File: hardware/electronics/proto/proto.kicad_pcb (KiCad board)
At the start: 2 copper layers, 47.9 x 53.5 mm, 49 parts, among them J1 Conn_01x08_Female, U1 ADS131M06IRSNT, U2 AP131-30

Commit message: Switch strain gauge footprints
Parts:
- R1, R10, R11, R12, R2, R3, R4, R5, R6, R7, R8, R9: value 1k -> 350; footprint Resistor_SMD:R_2512_6332Metric_Pad1.40x3.35mm_HandSolder -> proto:StrainGauge_BF350-3AA
- U1: value ADS131M06IRSNT -> ADS131M06

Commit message: Update layout and route
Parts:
- added R25: 3.9k, Resistor_SMD:R_0603_1608Metric_Pad0.98x0.95mm_HandSolder, F.Cu at (9.25, 4.95)
- added R26: 3.9k, Resistor_SMD:R_0603_1608Metric_Pad0.98x0.95mm_HandSolder, F.Cu at (9.25, -4.95)
- added R27: 3.9k, Resistor_SMD:R_0603_1608Metric_Pad0.98x0.95mm_HandSolder, F.Cu at (-0.34, -10.5)
- added R28: 3.9k, Resistor_SMD:R_0603_1608Metric_Pad0.98x0.95mm_HandSolder, F.Cu at (-8.91, -5.54)
- added R29: 3.9k, Resistor_SMD:R_0603_1608Metric_Pad0.98x0.95mm_HandSolder, F.Cu at (-8.91, 5.54)
- added R30: 3.9k, Resistor_SMD:R_0603_1608Metric_Pad0.98x0.95mm_HandSolder, F.Cu at (-0.34, 10.5)
- R13, R14, R15, R16, R17, R18, R19, R20, R21, R22, R23, R24: value 1k -> 8.2k
- moved R5 1.40 mm to (-6.07, -19.3), turned to 17.5 degrees
- moved R6 1.40 mm to (-6.07, -19.3), turned to -162.5 degrees
- moved R1 1.40 mm to (19.7, 4.37), turned to -102.5 degrees
- moved R2 1.40 mm to (19.7, 4.37), turned to 77.5 degrees
- moved R10 1.40 mm to (-13.6, 14.9), turned to -42.5 degrees
- moved R9 1.40 mm to (-13.6, 14.9), turned to 137.5 degrees
- moved R7 1.40 mm to (-13.6, -14.9), turned to 42.5 degrees
- moved R8 1.40 mm to (-13.6, -14.9), turned to -137.5 degrees
- moved R3 1.40 mm to (19.7, -4.37), turned to -77.5 degrees
- moved R4 1.40 mm to (19.7, -4.37), turned to 102.5 degrees
- moved R11 1.40 mm to (-6.07, 19.3), turned to 162.5 degrees
- moved R12 1.40 mm to (-6.07, 19.3), turned to -17.5 degrees
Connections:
- C1 pad 2: /BRa -> Net-(C1-Pad2)
- C2 pad 2: /BRb -> Net-(C2-Pad2)
- C3 pad 2: /BRc -> Net-(C3-Pad2)
- C4 pad 2: /BRd -> Net-(C4-Pad2)
- C5 pad 2: /BRe -> Net-(C5-Pad2)
- C6 pad 2: /BRf -> Net-(C6-Pad2)
- R11 pad 1: VDDA -> /BRf
- R11 pad 2: /BRf -> VDDA
- R12 pad 1: /BRf -> GNDA
- R12 pad 2: GNDA -> /BRf
- R3 pad 1: VDDA -> /BRb
- R3 pad 2: /BRb -> VDDA
- R4 pad 1: /BRb -> GNDA
- R4 pad 2: GNDA -> /BRb
- R7 pad 1: VDDA -> /BRd
- R7 pad 2: /BRd -> VDDA
- R8 pad 1: /BRd -> GNDA
- R8 pad 2: GNDA -> /BRd
- U1 pad 1: /BRc -> Net-(C3-Pad2)
- U1 pad 29: /BRa -> Net-(C1-Pad2)
- U1 pad 32: /BRb -> Net-(C2-Pad2)
- U1 pad 4: /BRd -> Net-(C4-Pad2)
- U1 pad 5: /BRe -> Net-(C5-Pad2)
- U1 pad 8: /BRf -> Net-(C6-Pad2)
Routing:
- net /BRa: track 34.6 -> 9.19 mm
- net Net-(C1-Pad2): track 0.00 -> 20.6 mm
- net /BRb: track 27.2 -> 9.19 mm
- net /BRc: track 24.8 -> 9.19 mm
- net /BRf: track 24.8 -> 9.19 mm
- net /BRe: track 23.5 -> 9.19 mm
- net /BRd: track 23.5 -> 9.19 mm
- net Net-(C2-Pad2): track 0.00 -> 13.2 mm
- net Net-(C6-Pad2): track 0.00 -> 10.8 mm
- net Net-(C3-Pad2): track 0.00 -> 10.8 mm
- net Net-(C4-Pad2): track 0.00 -> 9.55 mm
- net Net-(C5-Pad2): track 0.00 -> 9.55 mm
- net GNDA: track 67.6 -> 74.2 mm
- net VDDA: track 95.6 -> 102.0 mm

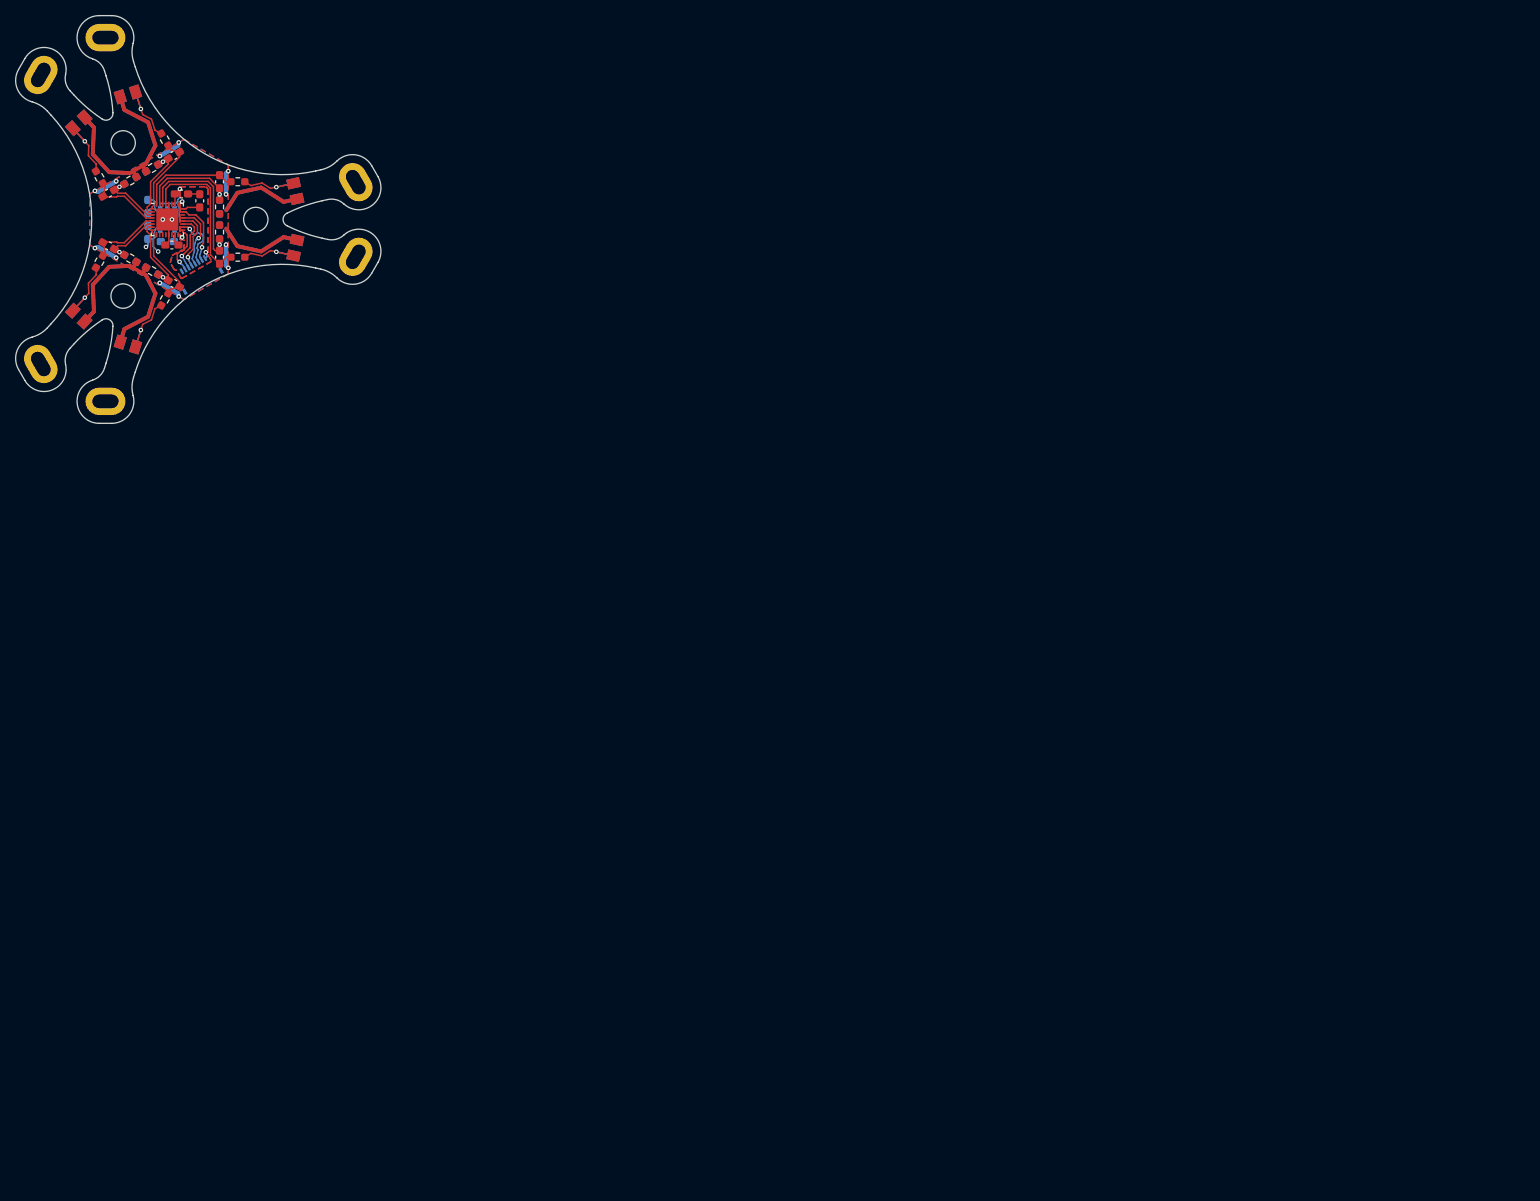
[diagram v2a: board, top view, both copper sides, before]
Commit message: Move prototype base PCB into center of sheet
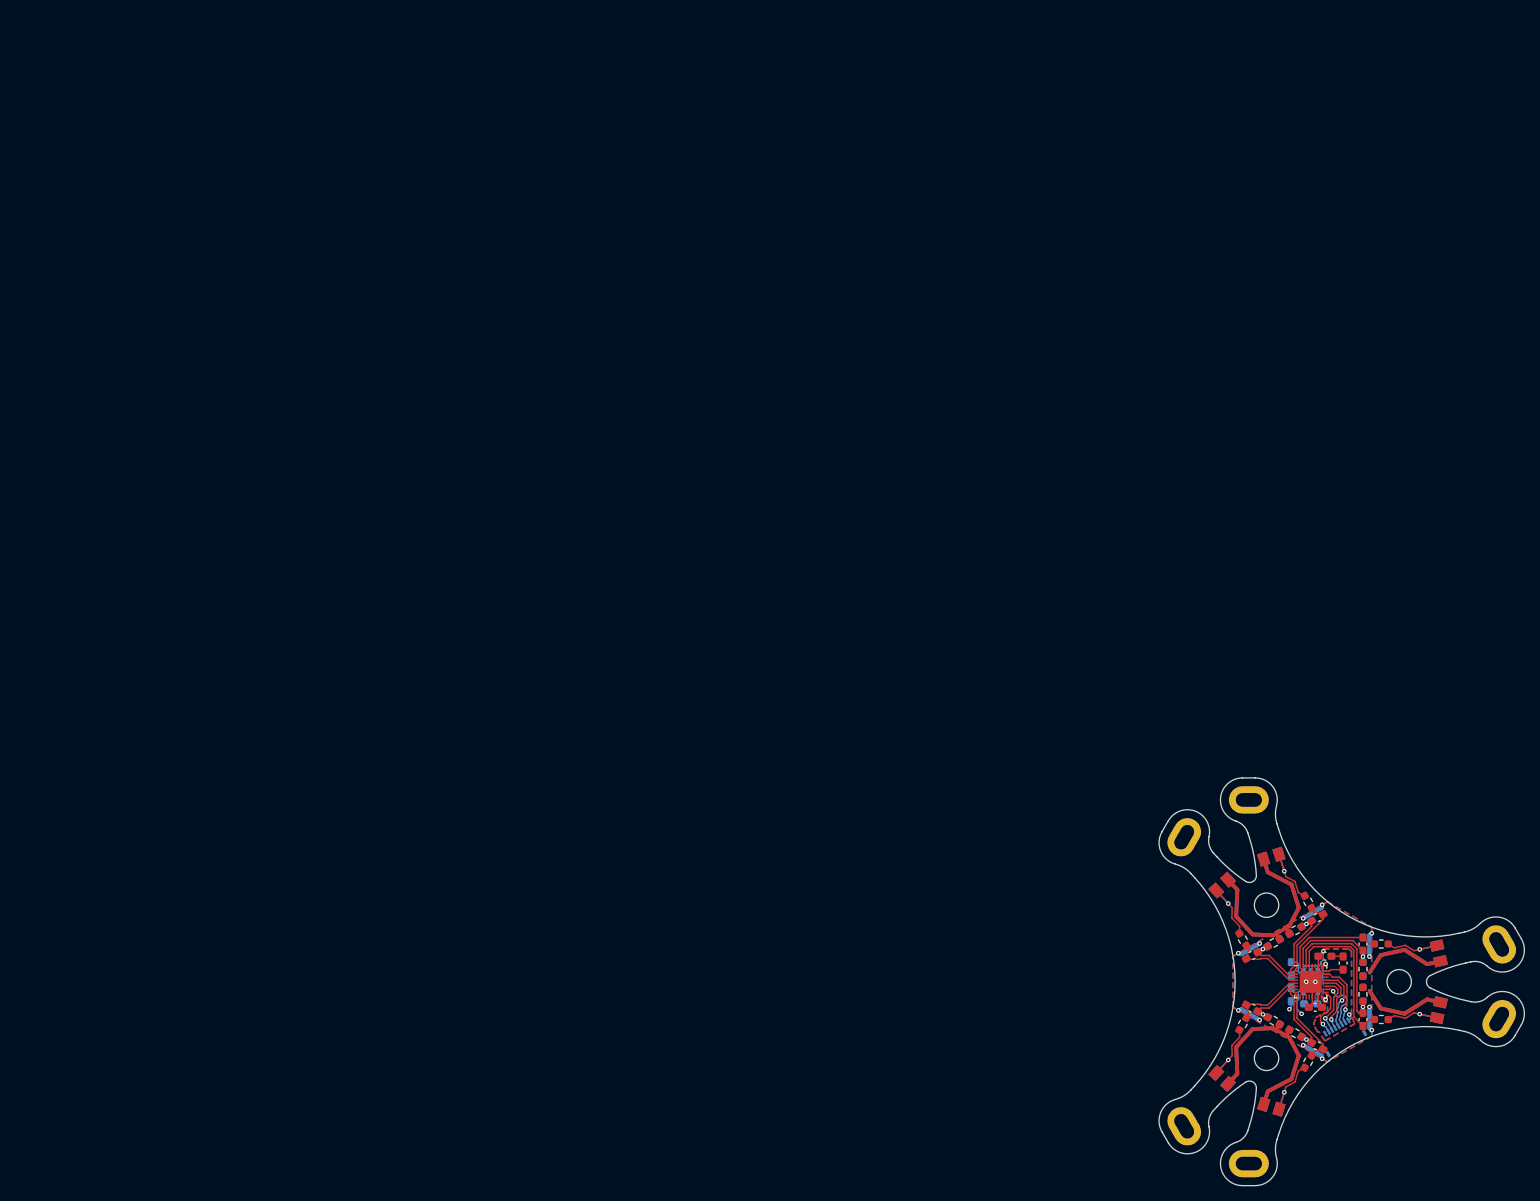
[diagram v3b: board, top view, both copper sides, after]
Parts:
- moved A1 180.3 mm to (174.4, 105.4)
- moved A2 180.3 mm to (174.4, 94.6)
- moved A3 180.3 mm to (142.5, 76.2)
- moved A4 180.3 mm to (133.1, 81.6)
- moved A5 180.3 mm to (133.1, 118.4)
- moved A6 180.3 mm to (142.5, 123.8)
- moved C1 180.3 mm to (156.9, 105.0)
- moved C10 180.3 mm to (147.5, 98.3)
- moved C11 180.3 mm to (150.0, 102.9)
- moved C12 180.3 mm to (147.4, 101.7)
- moved C2 180.3 mm to (156.8, 95.0)
- moved C3 180.3 mm to (150.9, 91.6)
- moved C4 180.3 mm to (142.3, 96.5)
- moved C5 180.3 mm to (142.3, 103.5)
- moved C6 180.3 mm to (150.9, 108.4)
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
